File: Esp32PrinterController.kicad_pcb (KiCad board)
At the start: 2 copper layers, 157.5 x 97.8 mm, 101 parts, among them J1 -24V IN+, J10 +NOZ-, J11 +BED-, J110 MOT X, J12 +FAN1-, J13 +FAN2-, J14 +FAN3-, J20 +BT-, J21 +NT-, J23 MOT Y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

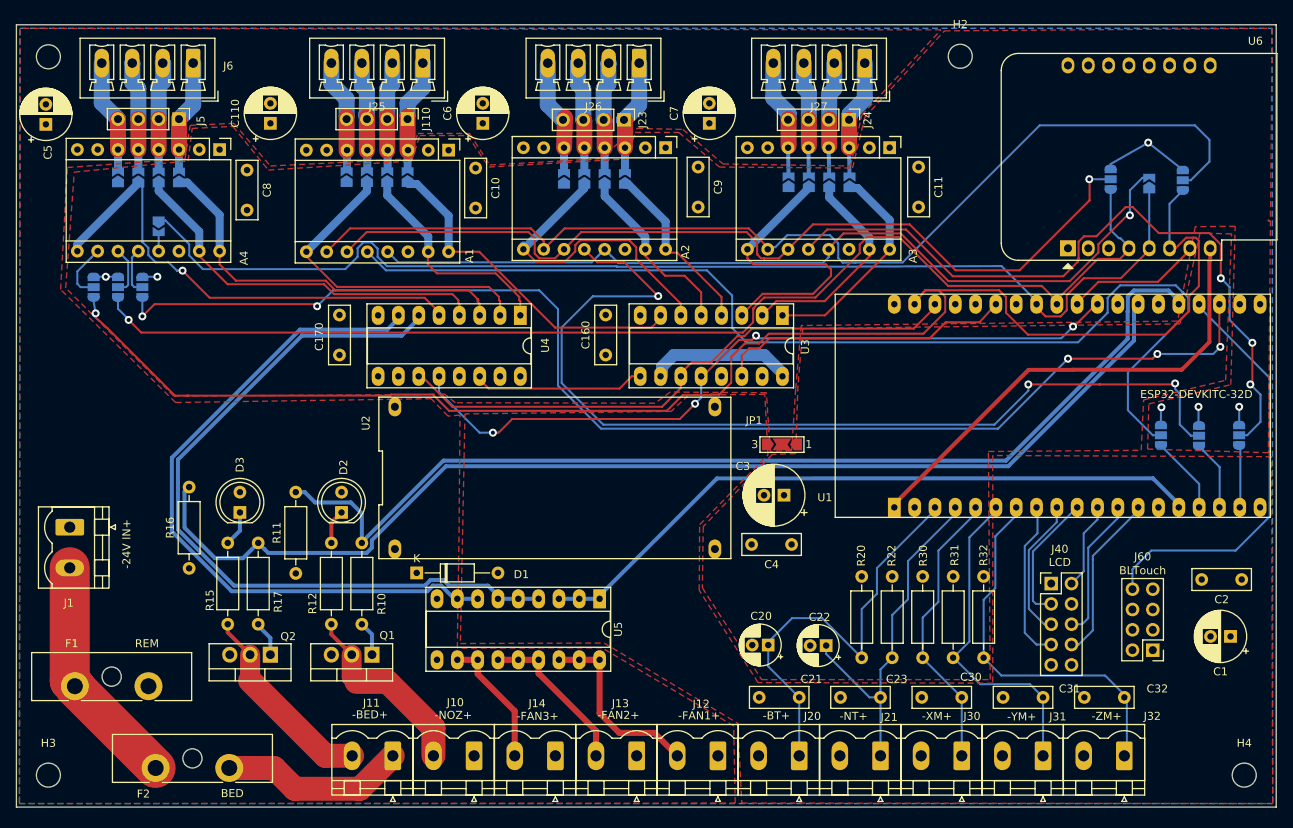
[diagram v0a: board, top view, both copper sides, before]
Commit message: Layout for D1 Mini form factor
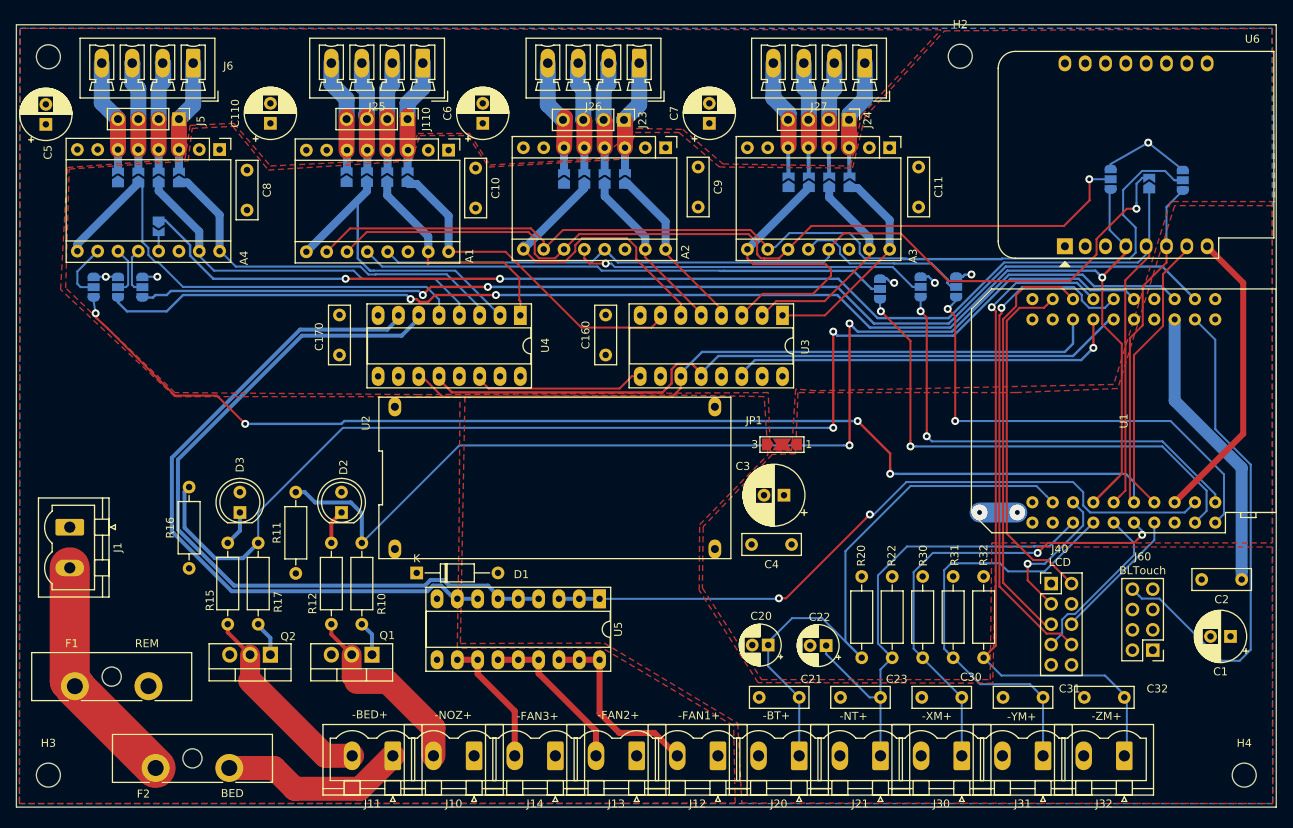
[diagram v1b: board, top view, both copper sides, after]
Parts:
- J1, J10, J11, J12, J13, J14, J20, J21, J30, J31, J32: footprint this:PhoenixContact_MSTBVA_2,5_2-G-5,08_1x02_P5.08mm_Vertical_WallToWall -> Connector_Phoenix_MSTB:PhoenixContact_MSTBVA_2,5_2-G-5,08_1x02_P5.08mm_Vertical
- U1: footprint this:MODULE_ESP32-DEVKITC-32D_LongPads -> Esp32Mini:Esp32MiniDevKitPinout
- moved JP27 39.9 mm to (142.9, 62.0)
- moved JP25 39.6 mm to (133.3, 62.2)
- moved JP26 39.5 mm to (138.4, 62.0)
- moved U1 7.89 mm to (162.6, 78.7)
- moved U6 0.46 mm to (156.5, 56.9)
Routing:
- net Net-(A2-Pad12): track 122.2 -> 44.6 mm, vias 3 -> 1
- net Net-(A1-Pad12): track 137.1 -> 66.0 mm
- net Net-(A3-Pad12): track 89.6 -> 22.2 mm, vias 3 -> 0
- net /CS_X: track 9.70 -> 63.9 mm, vias 0 -> 2
- net /CS_Z: track 7.83 -> 59.2 mm, vias 0 -> 2
- net /CS_Y: track 8.73 -> 57.8 mm, vias 0 -> 2
- net /IO12_LCD_EN: track 21.8 -> 64.0 mm, vias 0 -> 1
- net /IO32_Z_MIN: track 47.6 -> 86.6 mm, vias 0 -> 1
- net +5V: track 0.00 -> 36.0 mm
- net /IO25_BTN_EN2: track 18.1 -> 53.0 mm
- net /IO27_BTN_ENC: track 10.9 -> 44.2 mm
- net /SD_MISO: track 146.3 -> 174.7 mm, vias 0 -> 2
- net /SD_SCK: track 151.1 -> 175.9 mm, vias 1 -> 3
- net /IO34_X_MIN: track 35.8 -> 57.9 mm, vias 0 -> 2
- net /CS_E: track 161.0 -> 139.1 mm, vias 5 -> 2
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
